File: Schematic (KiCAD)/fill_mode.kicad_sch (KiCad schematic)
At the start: 10 parts

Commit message: - Started work on the pulse channels.  - Solved at least 2 of the red traces in the SVG.  - Finally realized that "Unknown 4to1" cells are actually just ordinary And-Or-Invert "AOI22" cells.
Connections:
- new net: L10. (/Q7), L15. (X)
- new net: L10. (/Q7), L14. (X)
- new net: L10. (/Q7), L16. (X)
- new net: L10. (/Q7), L13. (X)
- new net: L10. (/Q7), L18. (X)
- new net: L10. (/Q7), L17. (X)
- new net: L10. (/Q7), L11. (X)
- new net: L10. (/Q7), L12. (X)

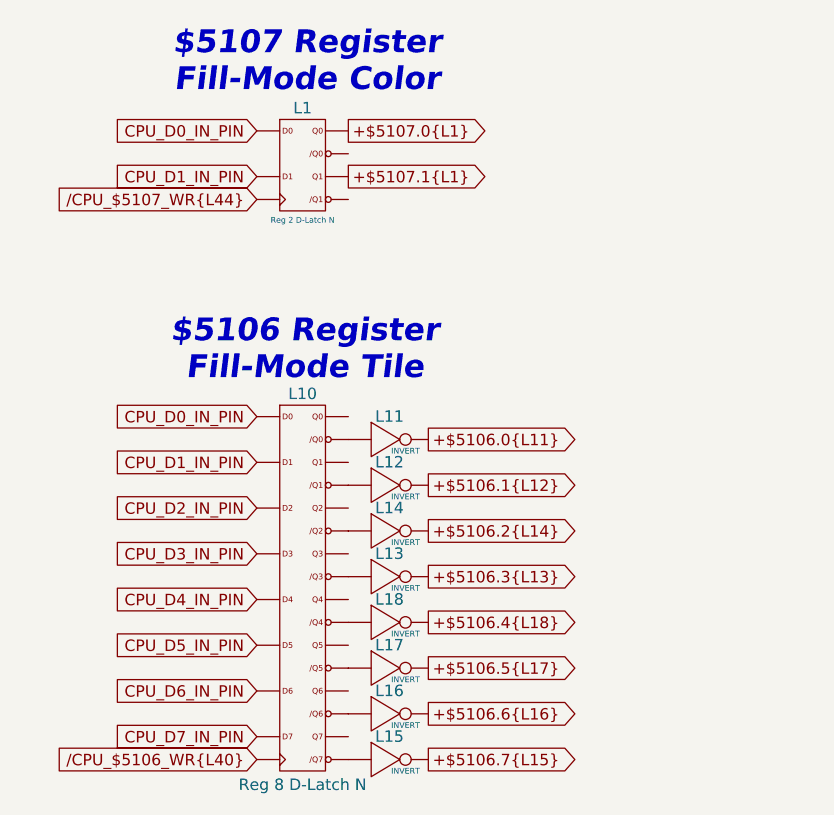
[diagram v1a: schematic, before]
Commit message: Schematic Updates:  - Added all 10-bit CHR banking registers $5120 - $512B, including where all 10 bits come from when written.  - Added 8-bit CHR bank register $5202, which is the bank used when rendering the V-Split region.    + V-Split seems to always be 8-bit, 8kB bank regardless of CHR mode.  The wiki doesn't say that and I don't know for sure.  - Added decoding logic that activates the correct CHR bank for CHR A10, A11, A12 (corresponding to columns AV, AW, AX).  - Noted, AX15 activates $5202 CHR Bank for V-Split region.  AX16 activates CHR Bank from data stored in ExRAM for extended attributes.  Therefore, AX15 driven by AT1 High means we specifically are in v-split region, and not extended attribute mode.  With this knowledge, backtracking up the chain from AT1 to N14 sheds very useful insight what the 3-bit shift register at N11/N12/N13 is doing.  We now know that N14 goes low specifically for pattern table fetches when rendering the V-split region, and does not appear dual-purposed for extended attribute fetch sequencing.  This may seem rather subtle or unimportant, but it is a good advancement for higher level understanding what that mysterious shift register might be doing.
SVG Trace Updates:
 - Registers $5120, 5121, 5122, 5123 (first 4 CHR bank register), the outputs were labeled in reverse order.
 - Register $5130 (highest CHR bank bits), the outputs were labeled with backwards polarity.  The error was not having taken into account that the CPU data bus input to the latches came already inverted to begin with.
 - Still wrong: Cell AV7, 2-input NAND gate.  One of the inputs is missing and it logically should be driven by AS19 like the 4 cells to its direct right.  I can't quite make out how it makes that connection.
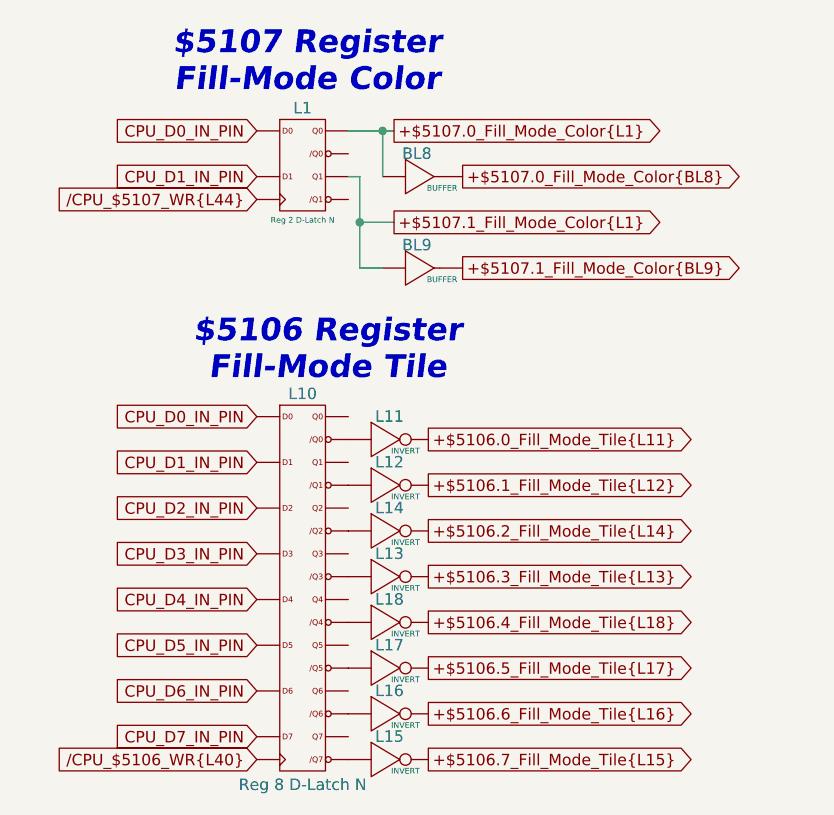
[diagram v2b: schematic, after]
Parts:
- added BL8, BL9: BUFFER, symbol MMC5:BUFFER
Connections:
- net +$5106.0{L11} is gone; now on net +$5106.0_Fill_Mode_Tile{L11}: L11. (X)
- net +$5106.1{L12} is gone; now on net +$5106.1_Fill_Mode_Tile{L12}: L12. (X)
- net +$5106.2{L14} is gone; now on net +$5106.2_Fill_Mode_Tile{L14}: L14. (X)
- net +$5106.3{L13} is gone; now on net +$5106.3_Fill_Mode_Tile{L13}: L13. (X)
- net +$5106.4{L18} is gone; now on net +$5106.4_Fill_Mode_Tile{L18}: L18. (X)
- net +$5106.5{L17} is gone; now on net +$5106.5_Fill_Mode_Tile{L17}: L17. (X)
- net +$5106.6{L16} is gone; now on net +$5106.6_Fill_Mode_Tile{L16}: L16. (X)
- net +$5106.7{L15} is gone; now on net +$5106.7_Fill_Mode_Tile{L15}: L15. (X)
- net +$5107.0{L1} is gone; now on net /CPU_$5107_WR{L44}: L1. (/Q1)
- net +$5107.1{L1} is gone; now on net /CPU_$5107_WR{L44}: L1. (/Q1)
- net +$5106.7_Fill_Mode_Tile{L15}: now reaches L15. (X)
- net +$5106.7_Fill_Mode_Tile{L15}: no longer L10. (/Q7)
- net +$5106.2_Fill_Mode_Tile{L14}: now reaches L14. (X)
- net +$5106.2_Fill_Mode_Tile{L14}: no longer L10. (/Q7)
- net +$5106.6_Fill_Mode_Tile{L16}: now reaches L16. (X)
- net +$5106.6_Fill_Mode_Tile{L16}: no longer L10. (/Q7)
- net +$5106.3_Fill_Mode_Tile{L13}: now reaches L13. (X)
- net +$5106.3_Fill_Mode_Tile{L13}: no longer L10. (/Q7)
- net +$5106.4_Fill_Mode_Tile{L18}: now reaches L18. (X)
- net +$5106.4_Fill_Mode_Tile{L18}: no longer L10. (/Q7)
- net +$5106.5_Fill_Mode_Tile{L17}: now reaches L17. (X)
- net +$5106.5_Fill_Mode_Tile{L17}: no longer L10. (/Q7)
- net +$5106.0_Fill_Mode_Tile{L11}: now reaches L11. (X)
- net +$5106.0_Fill_Mode_Tile{L11}: no longer L10. (/Q7)
- net +$5106.1_Fill_Mode_Tile{L12}: now reaches L12. (X)
- net +$5106.1_Fill_Mode_Tile{L12}: no longer L10. (/Q7)
- new net: L10. (/Q7), L15. (X)
- new net: L10. (/Q7), L14. (X)
- new net: L10. (/Q7), L16. (X)
- new net: L10. (/Q7), L13. (X)
- new net: L10. (/Q7), L18. (X)
- new net: L10. (/Q7), L17. (X)
- new net: L10. (/Q7), L11. (X)
- new net: L10. (/Q7), L12. (X)
- new net +$5107.0_Fill_Mode_Color{BL8}: BL8. (X)
- new net +$5107.0_Fill_Mode_Color{L1}: BL8. (X), L1. (/Q1)
- new net +$5107.1_Fill_Mode_Color{BL9}: BL9. (X)
- new net +$5107.1_Fill_Mode_Color{L1}: BL9. (X), L1. (/Q1)
